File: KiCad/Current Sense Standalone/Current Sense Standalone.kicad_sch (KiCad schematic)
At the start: 9 parts, among them J1 PLUG INPUT BATTERY IN HERE, J3 V+/- TEST Header PIN, J4 BAT +TERMINAL TEST HEADER PIN, J5 HEADER PIN FOR TEST, J6 to MCU GPIO PIN, J7 PLUG BATTERY OUTPUT HERE, U1 INA139QPWRQ1

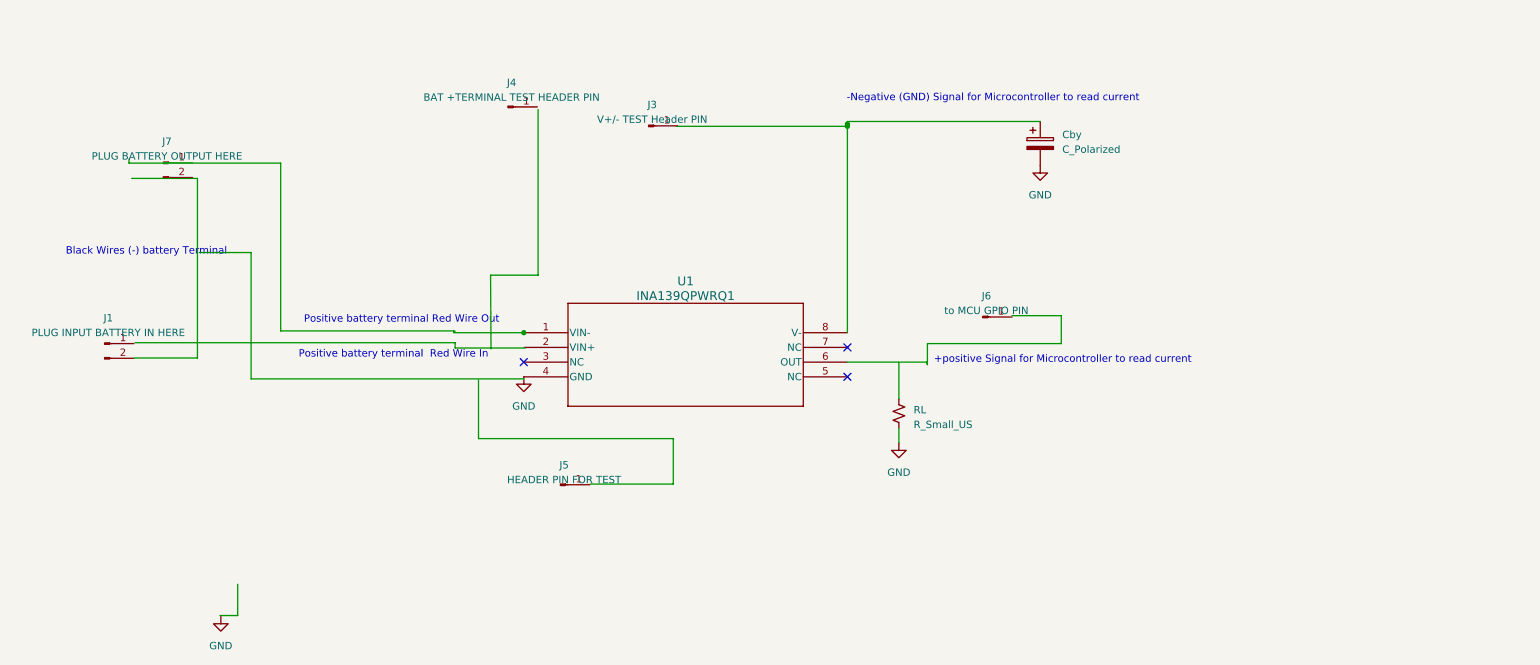
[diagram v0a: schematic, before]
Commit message: Current Sense Update
Added cap filter
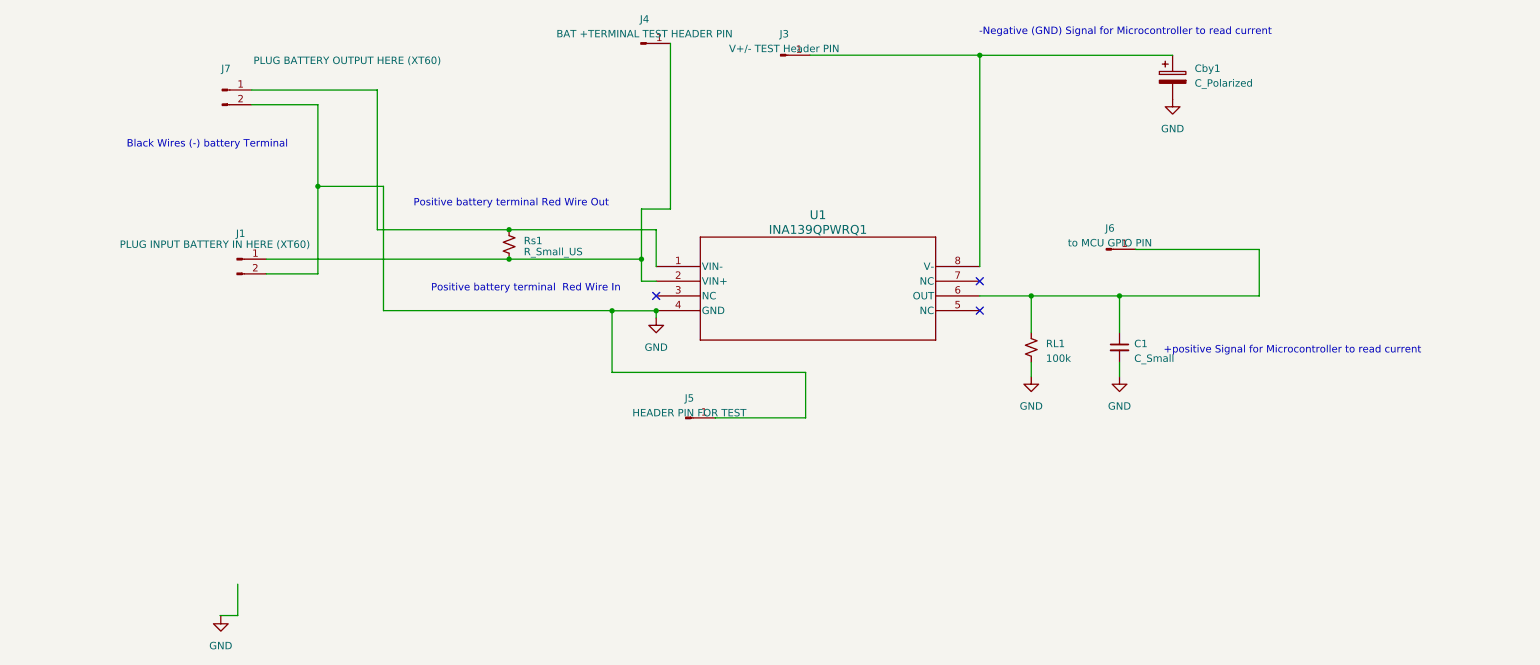
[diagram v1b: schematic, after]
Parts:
- added C1: C_Small, symbol Device:C_Small
- added Rs1: R_Small_US, Res_Bourns_CSS2H-3920R-L300F:Bourns-CSS2H-3920R-L300F-MFG, symbol Device:R_Small_US
- J1: value PLUG INPUT BATTERY IN HERE -> PLUG INPUT BATTERY IN HERE (XT60)
- J7: value PLUG BATTERY OUTPUT HERE -> PLUG BATTERY OUTPUT HERE (XT60)
- RL1: renamed from RL; value R_Small_US -> 100k
- renumbered Cby to Cby1
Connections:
- net GND: now also J1.2 (Pin_2), J5.1 (Pin_1), J7.2 (Pin_2), C1.2
- net at J3.1 (Pin_1): now also Cby1.1, U1.8 (V-)
- net at J6.1 (Pin_1): now also RL1.1, U1.6 (OUT), C1.1
- net at J7.1 (Pin_1): now also U1.1 (VIN-), Rs1.1
- net at J4.1 (Pin_1): now also J1.1 (Pin_1), U1.2 (VIN+), Rs1.2
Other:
- moved on the sheet: Cby1, J1, J3, J4, J5, J6, J7, RL1, U1

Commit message: Current Sense Update
Updated footprints for the headers. Just waiting on which capacitors we will use.
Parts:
- removed Cby1: C_Polarized, symbol Device:C_Polarized
- added C2: 0.1uF, symbol Device:C_Small
- C1: value C_Small -> 80pF
- J1: footprint (none) -> Mechatronic Footprints:AMASS_XT60-M_1x02_P7.20mm_Vertical
- J3, J4, J5, J6: footprint (none) -> Connector_PinHeader_2.54mm:PinHeader_1x02_P2.54mm_Vertical
- J7: footprint (none) -> Mechatronic Footprints:AMASS_XT60-F_1x02_P7.20mm_Vertical
- RL1: footprint (none) -> RC1206FR-13100KL:RESC3216X65
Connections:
- net GND: now also C2.2
- net at J3.1 (Pin_1), U1.8 (V-): now also C2.1
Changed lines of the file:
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@@
     (stroke (width 0) (type default))
   )
-  (wire (pts (xy 201.93 49.8856) (xy 235.2294 49.8856))
+  (wire (pts (xy 201.93 49.8856) (xy 235.3257 49.8856))
+    (stroke (width 0) (type default))
+  )
+  (wire (pts (xy 235.3257 55.6964) (xy 235.3257 57.1165))
     (stroke (width 0) (type default))
   )
@@
     (stroke (width 0) (type default))
   )
+  (wire (pts (xy 235.3257 50.6164) (xy 235.3257 49.8856))
+    (stroke (width 0) (type default))
+  )
   (image (at 81.3308 154.1272) (scale 0.926512)
     (data
@@
       (effects (font (size 1.27 1.27)))
     )
-    (property "Footprint" "" (at 167.5311 49.8673 0)
+    (property "Footprint" "Connector_PinHeader_2.54mm:PinHeader_1x02_P2.54mm_Vertical" (at 167.5311 49.8673 0)
       (effects (font (size 1.27 1.27)) hide)
     )
@@
       (effects (font (size 1.27 1.27)))
     )
-    (property "Footprint" "" (at 223.7753 83.3852 0)
+    (property "Footprint" "Connector_PinHeader_2.54mm:PinHeader_1x02_P2.54mm_Vertical" (at 223.7753 83.3852 0)
       (effects (font (size 1.27 1.27)) hide)
     )
@@
       (effects (font (size 1.27 1.27)) (justify left))
     )
-    (property "Footprint" "" (at 210.82 100.33 0)
+    (property "Footprint" "RC1206FR-13100KL:RESC3216X65" (at 210.82 100.33 0)
       (effects (font (size 1.27 1.27)) hide)
     )
@@
       (effects (font (size 1.27 1.27)))
     )
-    (property "Footprint" "" (at 71.12 55.88 0)
+    (property "Footprint" "Mechatronic Footprints:AMASS_XT60-F_1x02_P7.20mm_Vertical" (at 71.12 55.88 0)
       (effects (font (size 1.27 1.27)) hide)
     )
@@
       (effects (font (size 1.27 1.27)) (justify left))
     )
-    (property "Value" "C_Small" (at 228.6 102.2413 0)
+    (property "Value" "80pF" (at 228.6 102.2413 0)
       (effects (font (size 1.27 1.27)) (justify left))
     )
@@
       (effects (font (size 1.27 1.27)))
     )
-    (property "Footprint" "" (at 151.1493 112.505 0)
+    (property "Footprint" "Connector_PinHeader_2.54mm:PinHeader_1x02_P2.54mm_Vertical" (at 151.1493 112.505 0)
       (effects (font (size 1.27 1.27)) hide)
     )
@@
       (effects (font (size 1.27 1.27)))
     )
-    (property "Footprint" "" (at 143.4028 47.842 0)
+    (property "Footprint" "Connector_PinHeader_2.54mm:PinHeader_1x02_P2.54mm_Vertical" (at 143.4028 47.842 0)
       (effects (font (size 1.27 1.27)) hide)
     )
@@
     )
   )
-  (symbol (lib_id "Device:C_Polarized") (at 235.2294 53.6956 0) (unit 1)
-    (in_bom yes) (on_board yes) (dnp no) (fields_autoplaced)
-    (property "Reference" "Cby1" (at 239.0394 52.1716 0)
-      (effects (font (size 1.27 1.27)) (justify left))
-    )
-    (property "Value" "C_Polarized" (at 239.0394 54.7116 0)
-      (effects (font (size 1.27 1.27)) (justify left))
-    )
-    (property "Footprint" "" (at 236.1946 57.5056 0)
-      (effects (font (size 1.27 1.27)) hide)
-    )
-    (property "Datasheet" "~" (at 235.2294 53.6956 0)
-      (effects (font (size 1.27 1.27)) hide)
-    )
-    (pin "1")
-    (pin "2")
-    (instances
-      (project "Current Sense Standalone"
-        (path "/af3dddb2-191c-40a1-9395-0fad50eefcf8"
-          (reference "Cby1") (unit 1)
-        )
-      )
-    )
-  )
   (symbol (lib_id "INA139QPWRQ1-8-TSSOP:INA139QPWRQ1") (at 146.05 86.36 0) (unit 1)
     (in_bom yes) (on_board yes) (dnp no) (fields_autoplaced)
@@
     )
   )
+  (symbol (lib_id "Device:C_Small") (at 235.3257 53.1564 0) (unit 1)
+    (in_bom yes) (on_board yes) (dnp no) (fields_autoplaced)
+    (property "Reference" "C2" (at 238.76 52.5277 0)
+      (effects (font (size 1.27 1.27)) (justify left))
+    )
+    (property "Value" "0.1uF" (at 238.76 55.0677 0)
+      (effects (font (size 1.27 1.27)) (justify left))
+    )
+    (property "Footprint" "" (at 235.3257 53.1564 0)
+      (effects (font (size 1.27 1.27)) hide)
+    )
+    (property "Datasheet" "~" (at 235.3257 53.1564 0)
+      (effects (font (size 1.27 1.27)) hide)
+    )
+    (pin "1")
+    (pin "2")
+    (instances
+      (project "Current Sense Standalone"
+        (path "/af3dddb2-191c-40a1-9395-0fad50eefcf8"
+          (reference "C2") (unit 1)
+        )
+      )
+    )
+  )
   (symbol (lib_id "power:GND") (at 210.82 105.41 0) (unit 1)
     (in_bom yes) (on_board yes) (dnp no) (fields_autoplaced)
@@
     )
   )
-  (symbol (lib_id "power:GND") (at 235.2294 57.5056 0) (unit 1)
+  (symbol (lib_id "power:GND") (at 235.3257 57.1165 0) (unit 1)
     (in_bom yes) (on_board yes) (dnp no) (fields_autoplaced)
-    (property "Reference" "#PWR02" (at 235.2294 63.8556 0)
+    (property "Reference" "#PWR02" (at 235.3257 63.4665 0)
       (effects (font (size 1.27 1.27)) hide)
     )
-    (property "Value" "GND" (at 235.2294 62.5856 0)
+    (property "Value" "GND" (at 235.3257 62.1965 0)
       (effects (font (size 1.27 1.27)))
     )
-    (property "Footprint" "" (at 235.2294 57.5056 0)
+    (property "Footprint" "" (at 235.3257 57.1165 0)
       (effects (font (size 1.27 1.27)) hide)
     )
-    (property "Datasheet" "" (at 235.2294 57.5056 0)
+    (property "Datasheet" "" (at 235.3257 57.1165 0)
       (effects (font (size 1.27 1.27)) hide)
     )
@@
       (effects (font (size 1.27 1.27)))
     )
-    (property "Footprint" "" (at 73.66 85.09 0)
+    (property "Footprint" "Mechatronic Footprints:AMASS_XT60-M_1x02_P7.20mm_Vertical" (at 73.66 85.09 0)
       (effects (font (size 1.27 1.27)) hide)
     )

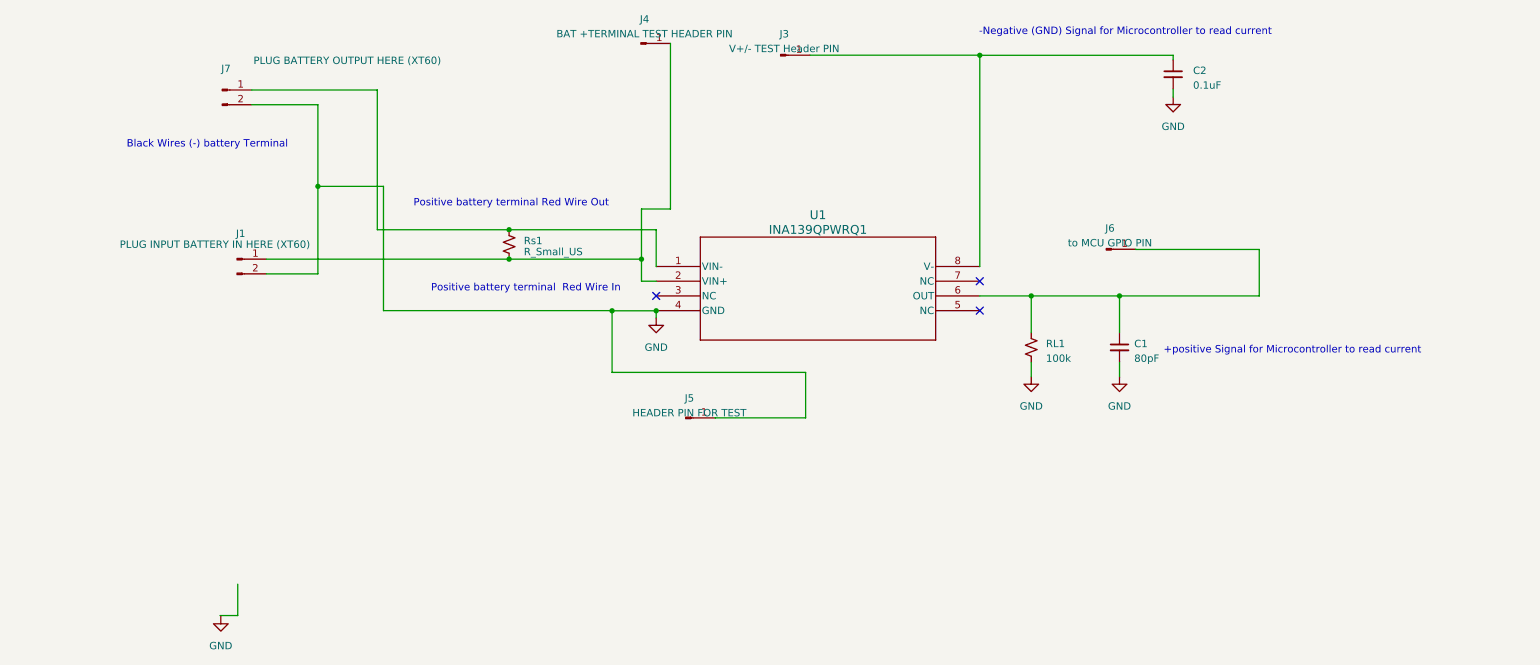
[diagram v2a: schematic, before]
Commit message: Current Sense
Updated PCB and Gerber Files
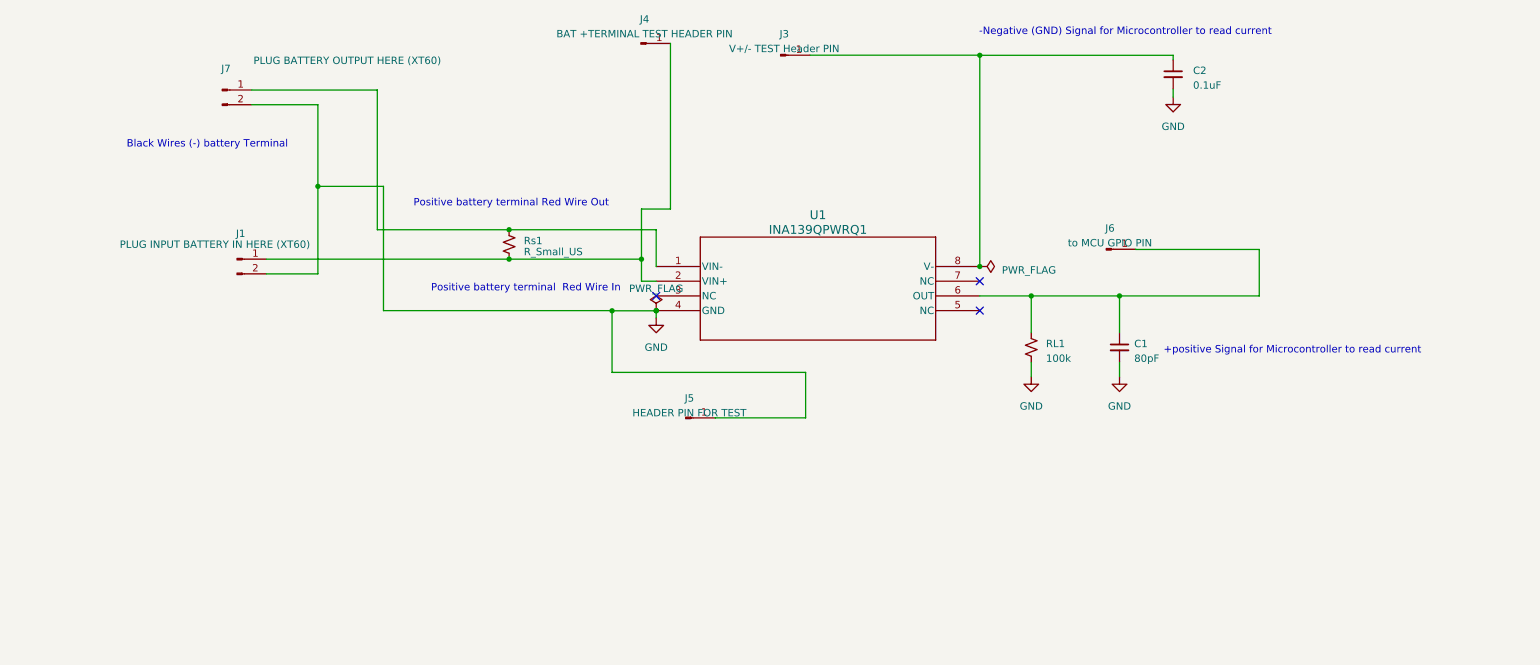
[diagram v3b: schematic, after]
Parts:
- C1, C2: footprint (none) -> Capacitor_SMD:C_1206_3216Metric
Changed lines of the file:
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@@
   (junction (at 146.05 94.006) (diameter 0) (color 0 0 0 0)
   )
+  (junction (at 146.05 93.98) (diameter 0) (color 0 0 0 0)
+  )
   (junction (at 201.93 49.8856) (diameter 0) (color 0 0 0 0)
   )
@@
   (junction (at 226.06 91.44) (diameter 0) (color 0 0 0 0)
   )
+  (junction (at 201.93 86.36) (diameter 0) (color 0 0 0 0)
+  )
   (junction (at 210.82 91.44) (diameter 0) (color 0 0 0 0)
   )
@@
     (stroke (width 0) (type default))
   )
-  (wire (pts (xy 73.787 141.224) (xy 73.787 146.6342))
-    (stroke (width 0) (type default))
-  )
   (wire (pts (xy 78.74 85.09) (xy 120.65 85.09))
     (stroke (width 0) (type default))
@@
     (stroke (width 0) (type default))
   )
-  (wire (pts (xy 70.7136 146.6342) (xy 73.787 146.6342))
-    (stroke (width 0) (type default))
-  )
   (wire (pts (xy 210.82 91.44) (xy 226.06 91.44))
     (stroke (width 0) (type default))
@@
     )
   )
+  (symbol (lib_id "power:PWR_FLAG") (at 146.05 93.98 0) (unit 1)
+    (in_bom yes) (on_board yes) (dnp no) (fields_autoplaced)
+    (property "Reference" "#FLG01" (at 146.05 92.075 0)
+      (effects (font (size 1.27 1.27)) hide)
+    )
+    (property "Value" "PWR_FLAG" (at 146.05 90.17 0)
+      (effects (font (size 1.27 1.27)))
+    )
+    (property "Footprint" "" (at 146.05 93.98 0)
+      (effects (font (size 1.27 1.27)) hide)
+    )
+    (property "Datasheet" "~" (at 146.05 93.98 0)
+      (effects (font (size 1.27 1.27)) hide)
+    )
+    (pin "1")
+    (instances
+      (project "Current Sense Standalone"
+        (path "/af3dddb2-191c-40a1-9395-0fad50eefcf8"
+          (reference "#FLG01") (unit 1)
+        )
+      )
+    )
+  )
   (symbol (lib_id "power:GND") (at 146.05 95.25 0) (unit 1)
     (in_bom yes) (on_board yes) (dnp no) (fields_autoplaced)
@@
       (effects (font (size 1.27 1.27)) (justify left))
     )
-    (property "Footprint" "" (at 226.06 100.33 0)
+    (property "Footprint" "Capacitor_SMD:C_1206_3216Metric" (at 226.06 100.33 0)
       (effects (font (size 1.27 1.27)) hide)
     )
@@
     )
   )
+  (symbol (lib_id "power:PWR_FLAG") (at 201.93 86.36 270) (unit 1)
+    (in_bom yes) (on_board yes) (dnp no) (fields_autoplaced)
+    (property "Reference" "#FLG02" (at 203.835 86.36 0)
+      (effects (font (size 1.27 1.27)) hide)
+    )
+    (property "Value" "PWR_FLAG" (at 205.74 86.995 90)
+      (effects (font (size 1.27 1.27)) (justify left))
+    )
+    (property "Footprint" "" (at 201.93 86.36 0)
+      (effects (font (size 1.27 1.27)) hide)
+    )
+    (property "Datasheet" "~" (at 201.93 86.36 0)
+      (effects (font (size 1.27 1.27)) hide)
+    )
+    (pin "1")
+    (instances
+      (project "Current Sense Standalone"
+        (path "/af3dddb2-191c-40a1-9395-0fad50eefcf8"
+          (reference "#FLG02") (unit 1)
+        )
+      )
+    )
+  )
   (symbol (lib_id "INA139QPWRQ1-8-TSSOP:INA139QPWRQ1") (at 146.05 86.36 0) (unit 1)
     (in_bom yes) (on_board yes) (dnp no) (fields_autoplaced)
@@
       (effects (font (size 1.27 1.27)) (justify left))
     )
-    (property "Footprint" "" (at 235.3257 53.1564 0)
+    (property "Footprint" "Capacitor_SMD:C_1206_3216Metric" (at 235.3257 53.1564 0)
       (effects (font (size 1.27 1.27)) hide)
     )
@@
         )
       )
-    )
-  )
-  (symbol (lib_id "power:GND") (at 70.866 146.7866 0) (unit 1)
-    (in_bom yes) (on_board yes) (dnp no) (fields_autoplaced)
-    (property "Reference" "#PWR04" (at 70.866 153.1366 0)
-      (effects (font (size 1.27 1.27)) hide)
-    )
-    (property "Value" "GND" (at 70.866 151.8666 0)
-      (effects (font (size 1.27 1.27)))
-    )
-    (property "Footprint" "" (at 70.866 146.7866 0)
-      (effects (font (size 1.27 1.27)) hide)
-    )
-    (property "Datasheet" "" (at 70.866 146.7866 0)
-      (effects (font (size 1.27 1.27)) hide)
-    )
-    (pin "1")
-    (instances
-      (project "Current Sense Standalone"
-        (path "/af3dddb2-191c-40a1-9395-0fad50eefcf8"
-          (reference "#PWR04") (unit 1)
-        )
-      )
